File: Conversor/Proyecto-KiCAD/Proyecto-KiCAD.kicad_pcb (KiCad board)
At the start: 2 copper layers, 139 parts, among them J1 ConnPila, J2 ConnTrafoP, J3 ConnTrafoS, J4 ConnLf, J5 ConnCarga, J6 Barrel_Jack_Switch, J7 DIMM100, P1 SW_SPDT, P10 Header GPIO, P11 Header SD, P12 USB-B, P2 5V Header, P3 5V Header, P4 Jumper 2, P5 Header 7X2, P6 Header UART, P7 Header I2C, P8 Header PWM, P9 Header ADC, Q1 IRFP150, Q2 IRFP150, Q3 IRFP150, Q4 IRFP150, Q5 IRF7425, SW1 Switch, SW2 Switch, SW3 Switch, SW4 Switch, SW5 Switch, U1 LP2985-3.3, U10 OPA365xxD, U11 LM7805_TO252, U12 ACPL-P480, U13 THB3-1211, U14 FT232BL, U15 LP2985-3.3, U2 ACPL-P480, U3 ACPL-P480, U4 ACPL-P480, U5 2ED21834-S06J, U6 2ED21834-S06J, U7 TMCS1100A4, U8 LM5056APMH/NOPB, U9 ISO7242C, Y1 6 MHz

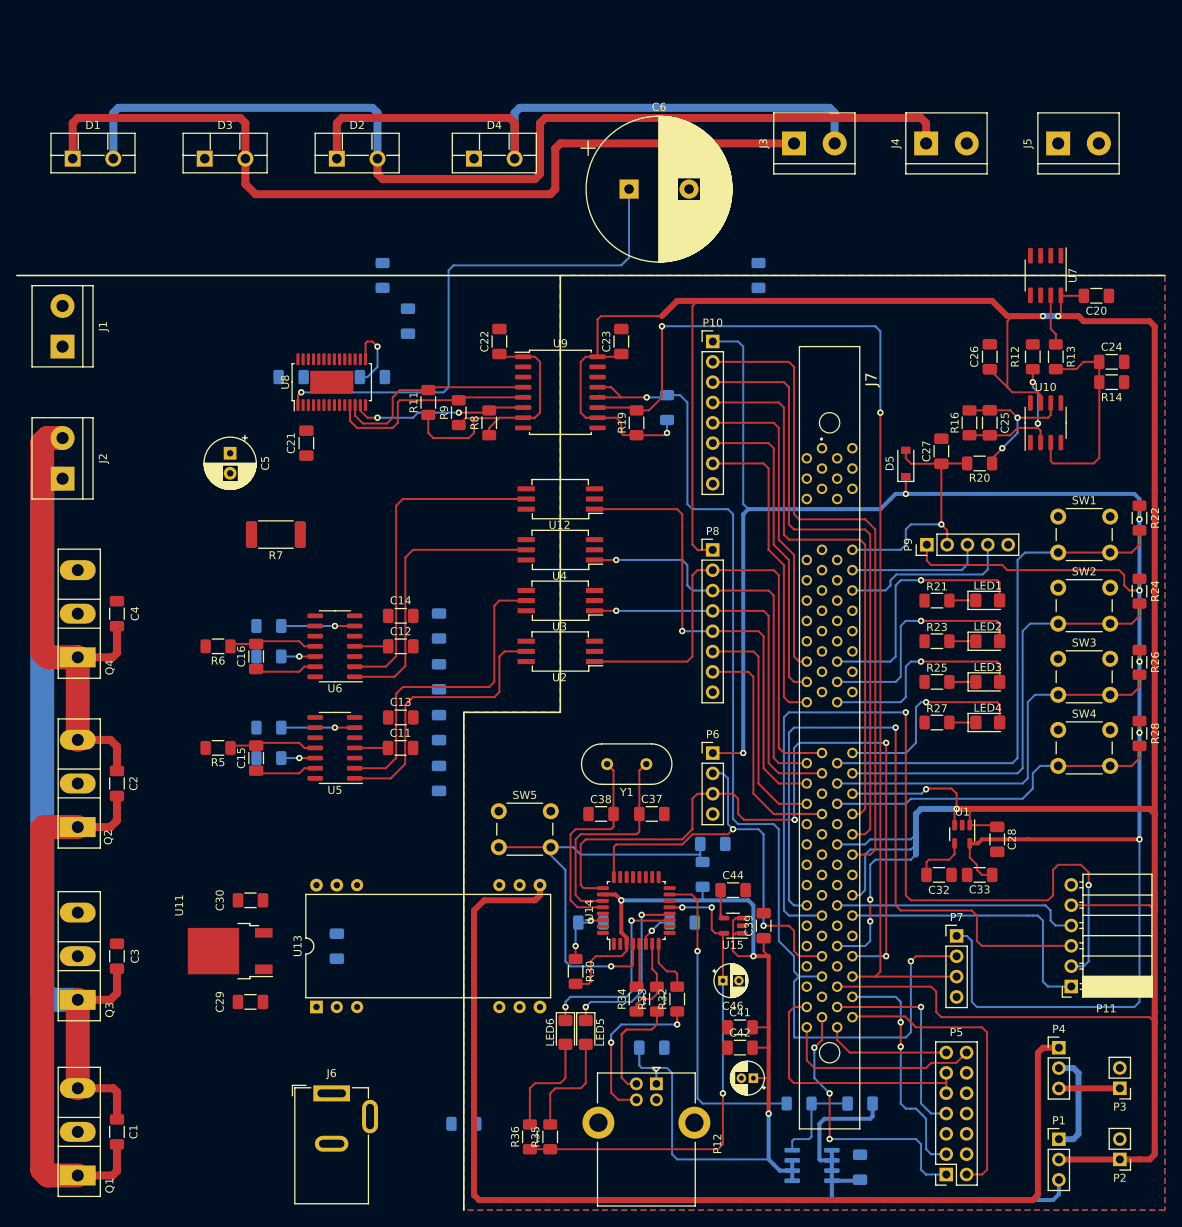
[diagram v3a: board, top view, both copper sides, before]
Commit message: Continuar con el diseño de la PCB
- Agregar los agujeros de tornillos
- Terminar la parte del secundario
- Agregar el borde en Egde.cuts que causaba problema
- Corregir las pista que no entran derechas a los pads
- Cambiar las footprints de los conectores
Por hacer:
  - Consultar de componentes como headers a Claus
  - Una vez terminada pedir cotización en las paginas que me pasó Jorge (Bookmarks de Firefox)
  - Ver de agrear un selector para la alimentación externa por header en la entrada de 12-18V (preguntar a Claus)
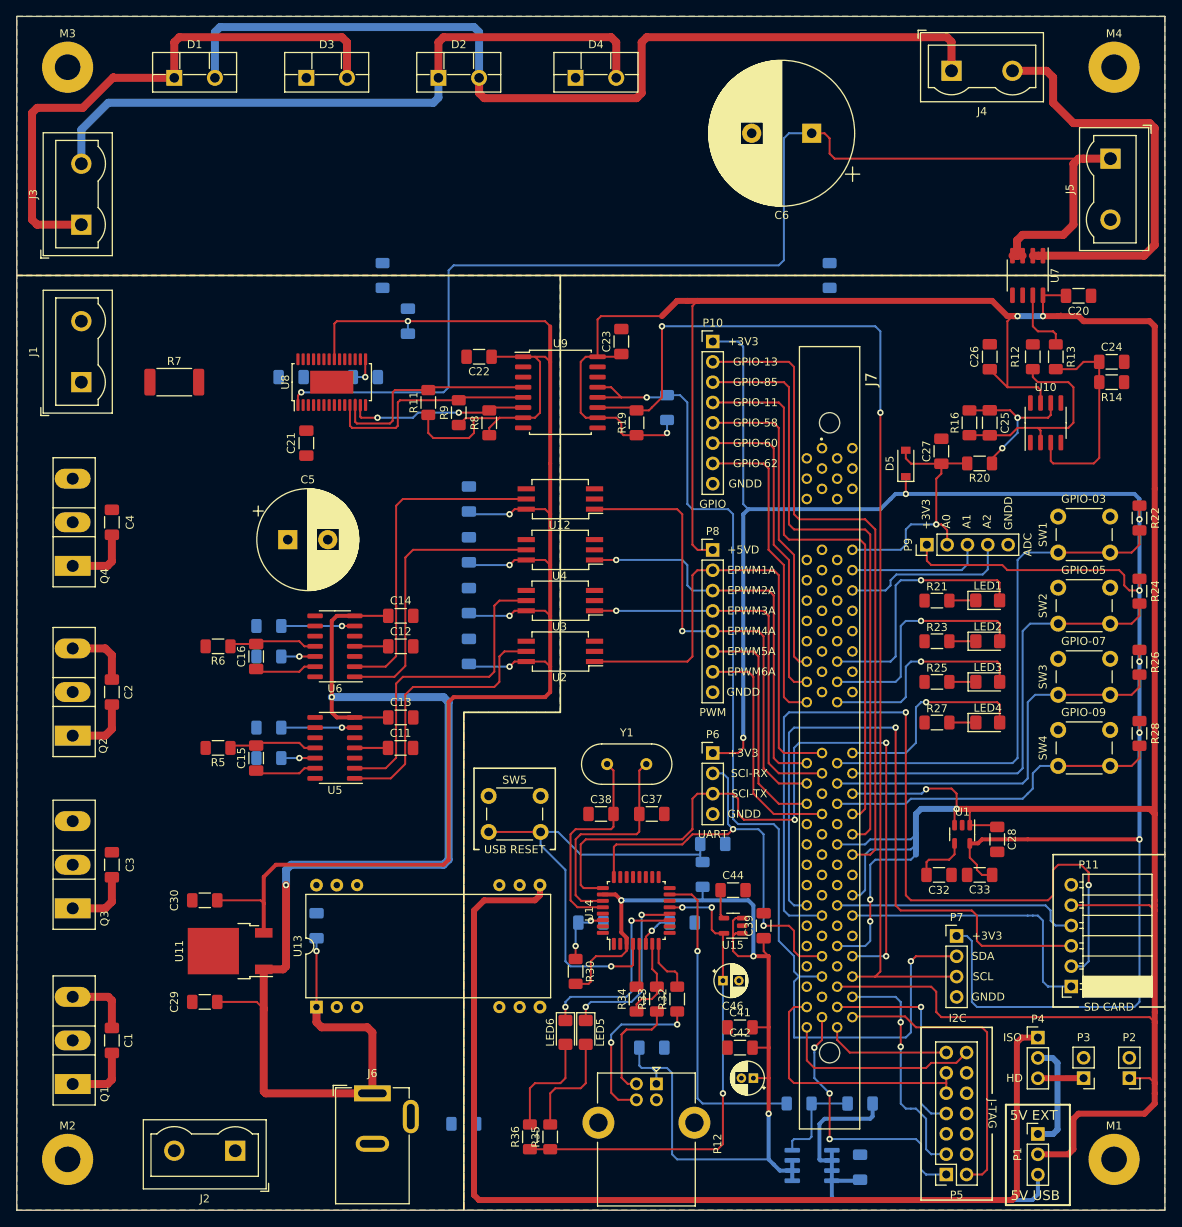
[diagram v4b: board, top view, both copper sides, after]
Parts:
- added M1: MountingHole_3.2mm_M3_Pad, MountingHole:MountingHole_3.2mm_M3_Pad, F.Cu at (161.3, 160.7)
- added M2: MountingHole_3.2mm_M3_Pad, MountingHole:MountingHole_3.2mm_M3_Pad, F.Cu at (30.5, 160.7)
- added M3: MountingHole_3.2mm_M3_Pad, MountingHole:MountingHole_3.2mm_M3_Pad, F.Cu at (30.5, 24.1)
- added M4: MountingHole_3.2mm_M3_Pad, MountingHole:MountingHole_3.2mm_M3_Pad, F.Cu at (161.3, 24.1)
- C5: footprint Capacitor_THT:CP_Radial_D6.3mm_P2.50mm -> Capacitor_THT:CP_Radial_D12.5mm_P5.00mm
- J1, J2, J3, J4, J5: footprint TerminalBlock:TerminalBlock_bornier-2_P5.08mm -> TerminalBlock:TerminalBlock_Wuerth_691311400102_P7.62mm
- moved J3 89.7 mm to (32.2, 43.8), turned to 90 degrees
- moved J2 86.7 mm to (51.4, 159.6), turned to 180 degrees
- moved C6 23.9 mm to (123.5, 32.4), turned to 180 degrees
- moved R7 22.9 mm to (43.8, 63.5), turned to 0 degrees
- moved C10 16.3 mm to (80.6, 78.1), turned to 90 degrees
- moved C7 16.3 mm to (80.6, 97.2), turned to 90 degrees
- moved C8 16.3 mm to (80.6, 90.8), turned to 90 degrees
- moved C9 16.3 mm to (80.6, 84.5), turned to 90 degrees
- moved D1 16.2 mm to (43.8, 25.5)
- moved D3 16.2 mm to (60.3, 25.5)
- moved D4 16.2 mm to (94.0, 25.5)
- moved D2 16.2 mm to (76.8, 25.5)
- moved C5 13.0 mm to (58.0, 83.2), turned to 0 degrees
- moved C1 11.4 mm to (36.0, 145.8)
- moved C2 11.4 mm to (36.0, 102.2)
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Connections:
- C18 pad 2: Net-(C18-Pad2) -> GND1
- U8 pad 21: Net-(C18-Pad2) -> +5VP
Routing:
- net +5VP: track 35.7 -> 231.0 mm, vias 0 -> 5
- net VDDA: track 0.00 -> 157.2 mm, vias 0 -> 3
- net /Conversor/S2D4: track 159.7 -> 16.8 mm
- net /Conversor/VLOAD/ILF-: track 66.8 -> 156.4 mm
- net /Conversor/ILF+: track 0.00 -> 53.0 mm
- net /Conversor/IFC-: track 68.6 -> 16.8 mm
- net Net-(D1-Pad1): track 108.9 -> 70.4 mm
- net /Conversor/S1D3: track 0.00 -> 16.8 mm
- net Net-(D1-Pad2): track 125.4 -> 116.9 mm
- net Net-(C25-Pad1): track 18.5 -> 26.7 mm, vias 2 -> 0
- net Net-(C19-Pad1): track 9.11 -> 3.80 mm
- net +5VD: track 432.5 -> 437.6 mm
- net /Placa DSP/USB-UART/RESET#: track 54.0 -> 58.5 mm
- net Net-(D2-Pad1): track 81.7 -> 84.7 mm
- net Net-(R13-Pad1): track 6.40 -> 8.44 mm
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- added copper zone on B.Cu, net GND1
- added copper zone on F.Cu, net GND1
- added copper zone on B.Cu, net GND2
- added copper zone on F.Cu, net GND2
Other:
- board outline added: 143.5 x 149.2 mm
- board text added: "+3V3"
- board text added: "+5VD"
- board text added: "5V EXT"
- board text added: "5V USB"
- board text added: "A0"
- board text added: "A1"
- board text added: "A2"
- board text added: "ADC"
- board text added: "EPWM1A"
- board text added: "EPWM2A"
- board text added: "EPWM3A"
- board text added: "EPWM4A"
- board text added: "EPWM5A"
- board text added: "EPWM6A"
- board text added: "GNDD"
- board text added: "GPIO"
- board text added: "GPIO-03"
- board text added: "GPIO-05"
- board text added: "GPIO-07"
- board text added: "GPIO-09"
- board text added: "GPIO-11"
- board text added: "GPIO-13"
- board text added: "GPIO-58"
- board text added: "GPIO-60"
- board text added: "GPIO-62"
- board text added: "GPIO-85"
- board text added: "HD"
- board text added: "I2C"
- board text added: "ISO"
- board text added: "J-TAG"
- board text added: "PWM"
- board text added: "SCI-RX"
- board text added: "SCI-TX"
- board text added: "SCL"
- board text added: "SD CARD"
- board text added: "SDA"
- board text added: "UART"
- board text added: "USB RESET"

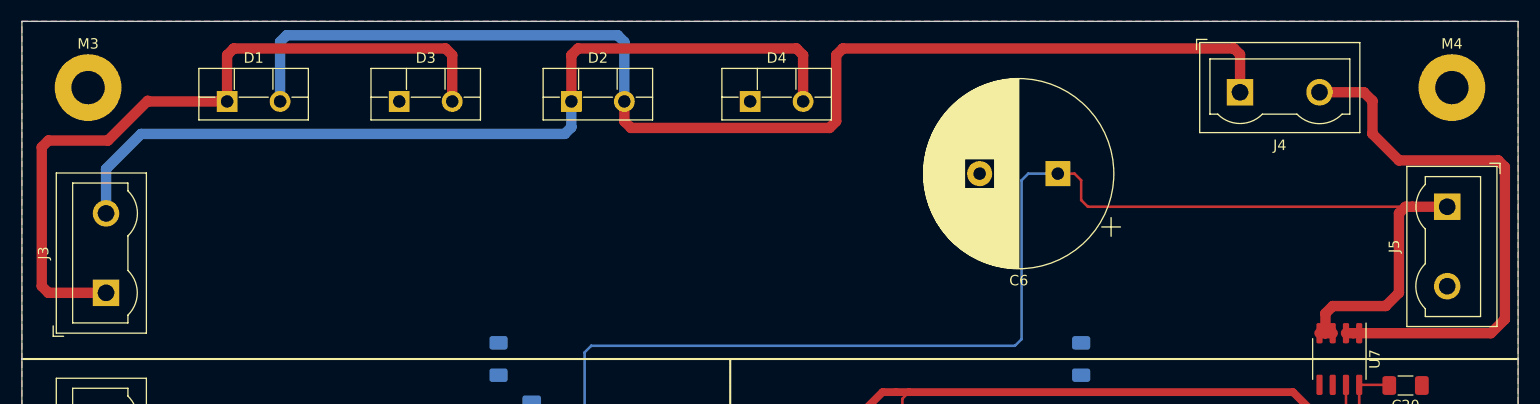
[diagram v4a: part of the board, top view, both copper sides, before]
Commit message: Cambiar el grosor de las pistas del primario de 1mm a 1.5mm
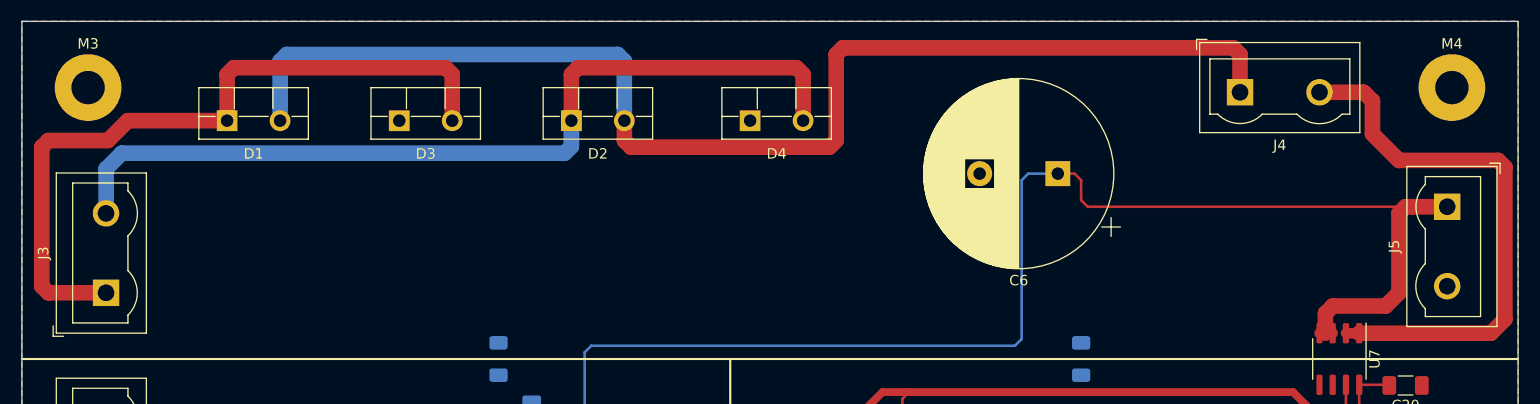
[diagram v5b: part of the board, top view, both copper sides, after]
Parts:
- moved D1 1.84 mm to (43.8, 27.3)
- moved D2 1.84 mm to (76.8, 27.3)
- moved D3 1.84 mm to (60.3, 27.3)
- moved D4 1.84 mm to (94.0, 27.3)
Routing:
- net Net-(D1-Pad2): track 116.9 -> 118.9 mm
- net Net-(D2-Pad1): track 84.7 -> 83.9 mm
- net Net-(D1-Pad1): track 70.4 -> 69.7 mm

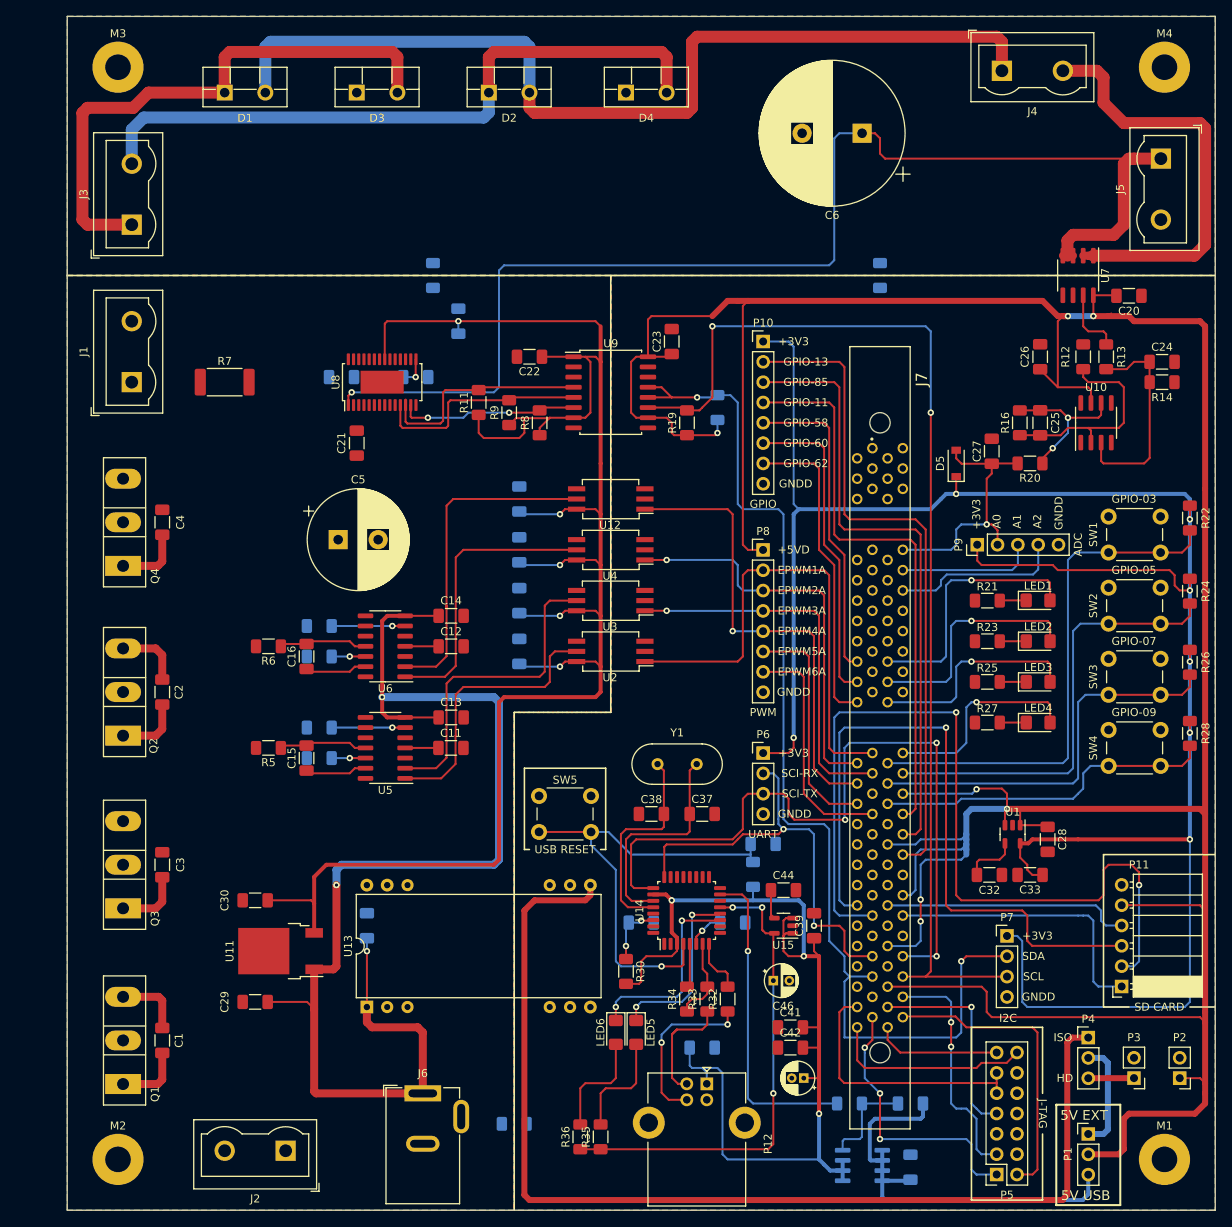
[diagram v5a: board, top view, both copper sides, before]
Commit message: Terminar de rutear todas las pistas de cobre de la placa
- Pistas de 4.5mm para las partes de 9A (primario) y 2mm para las de 4A (secundario)
- Agregar doble capacitor en serie a la salida, para disminuir los requerimientos de tensión de cada capacitor
  - Falta ver si es necesario a la entrada
- Agregar el circuito de medición de corriente a la entrada como recomienda la hoja de datos del LM5056
- Agregar modelos 3D de los conectores (sacados de Irusta-Caravelli)
Por hacer:
  - Preguntar por los componentes disponibles a Claus
  - Ver como entran los disipadores para MOSFETs y diodos
  - Asegurarse de la conexión de las dos líneas de datos de I2C despues del aislador
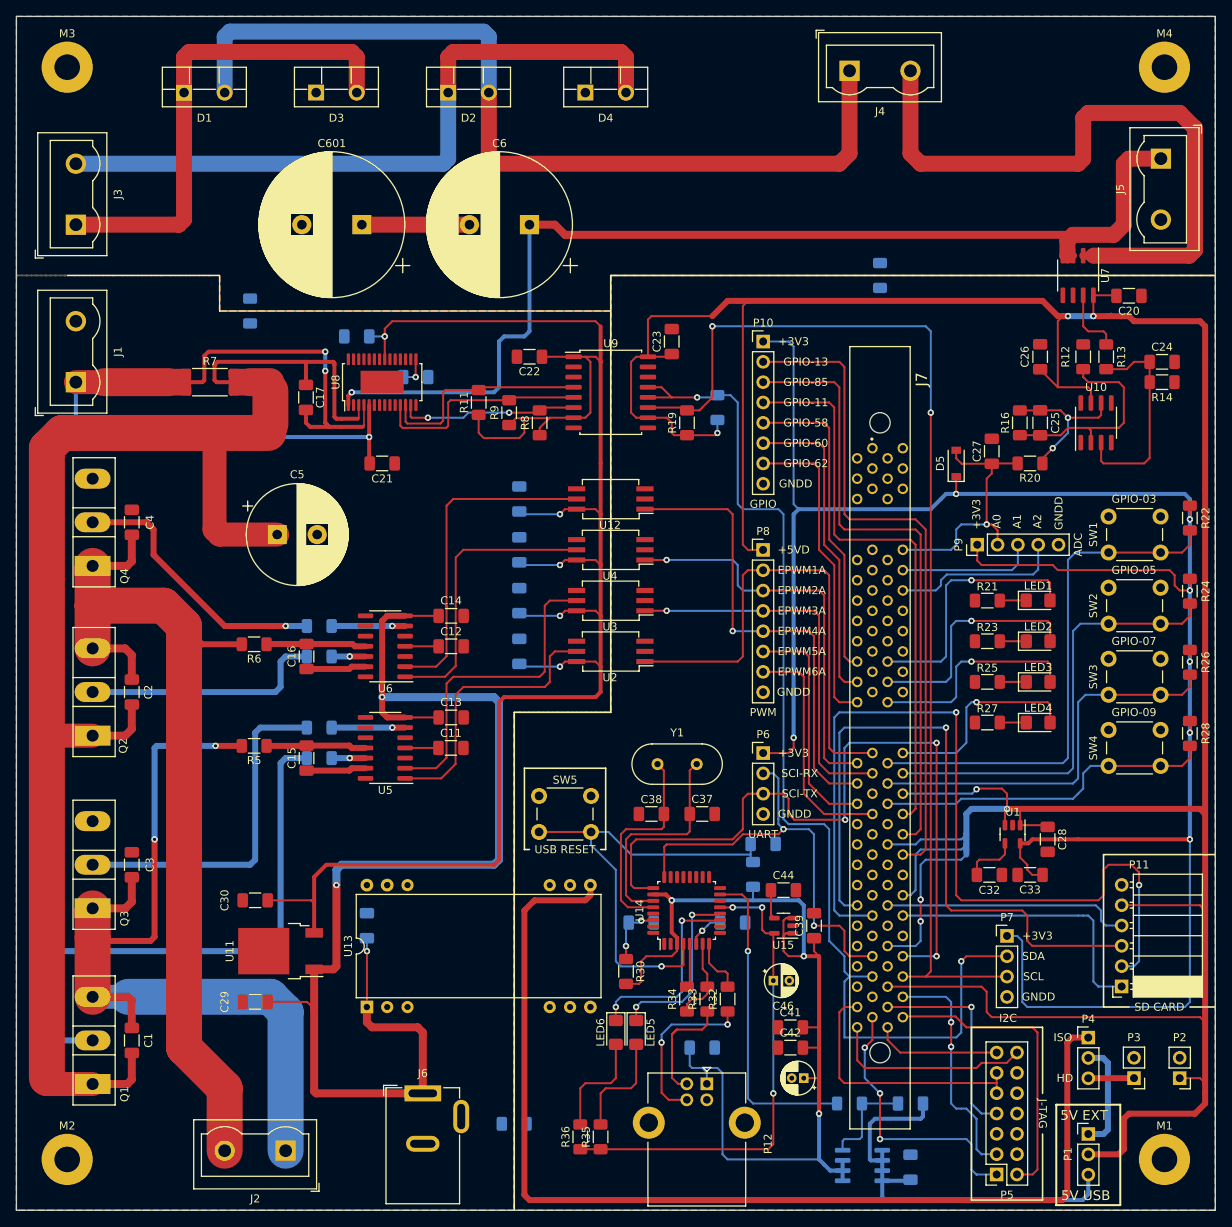
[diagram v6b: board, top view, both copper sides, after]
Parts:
- added C601: Cf2, Capacitor_THT:CP_Radial_D18.0mm_P7.50mm, F.Cu at (61.0, 43.8)
- C17: moved to F.Cu
- C6: value Cf -> Cf1
- moved C6 43.1 mm to (81.9, 43.8)
- moved R17 23.3 mm to (47.0, 54.6)
- moved J4 19.0 mm to (121.9, 24.6)
- moved C18 12.8 mm to (60.3, 57.8), turned to 180 degrees
- moved C5 7.65 mm to (50.4, 82.5)
- moved J1 6.99 mm to (25.2, 63.5)
- moved J3 6.99 mm to (25.2, 43.8)
- moved M2 6.35 mm to (24.1, 160.7)
- moved M3 6.35 mm to (24.1, 24.1)
- moved C17 5.12 mm to (54.0, 65.4), turned to 90 degrees
- moved D3 5.08 mm to (55.2, 27.3)
- moved D1 5.08 mm to (38.7, 27.3)
- moved D2 5.08 mm to (71.8, 27.3)
- moved D4 5.08 mm to (88.9, 27.3)
- moved C21 4.07 mm to (63.5, 73.7), turned to 0 degrees
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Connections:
- C6 pad 2: GND2 -> Net-(C6-Pad2)
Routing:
- net /Conversor/IFC-: track 16.8 -> 227.2 mm
- net /Conversor/IFC+: track 0.00 -> 134.4 mm, vias 0 -> 3
- net /Conversor/S2D4: track 16.8 -> 115.4 mm
- net /Conversor/S1D3: track 16.8 -> 112.9 mm, vias 0 -> 2
- net /Conversor/GATE1: track 0.00 -> 70.3 mm
- net /Conversor/GATE3: track 0.00 -> 43.2 mm
- net /Conversor/GATE4: track 0.00 -> 34.0 mm, vias 0 -> 1
- net /Conversor/GATE2: track 0.00 -> 30.5 mm
- net /Conversor/ILF+: track 53.0 -> 82.3 mm
- net /Conversor/VLOAD/ILF-: track 156.4 -> 135.9 mm
- net Net-(C6-Pad2): track 0.00 -> 13.5 mm
- net Net-(D1-Pad1): track 69.7 -> 60.7 mm
- net Net-(D1-Pad2): track 118.9 -> 112.0 mm
- net Net-(D2-Pad1): track 83.9 -> 86.7 mm
- net Net-(C16-Pad2): track 11.1 -> 13.0 mm
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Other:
- board size 143.5 x 149.2 mm -> 149.9 x 149.2 mm
